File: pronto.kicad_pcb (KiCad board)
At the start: 2 copper layers, 53.3 x 81.3 mm, 400 parts

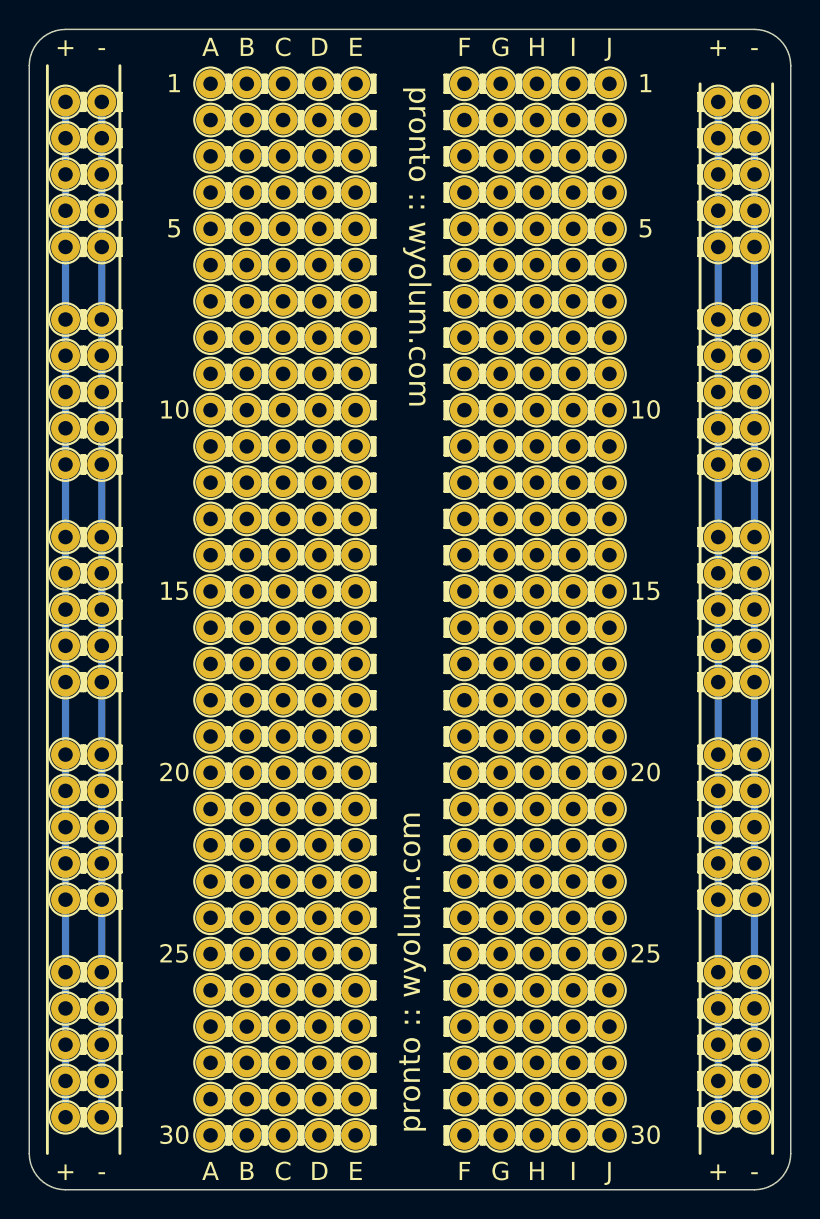
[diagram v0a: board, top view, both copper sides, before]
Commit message: front legend update
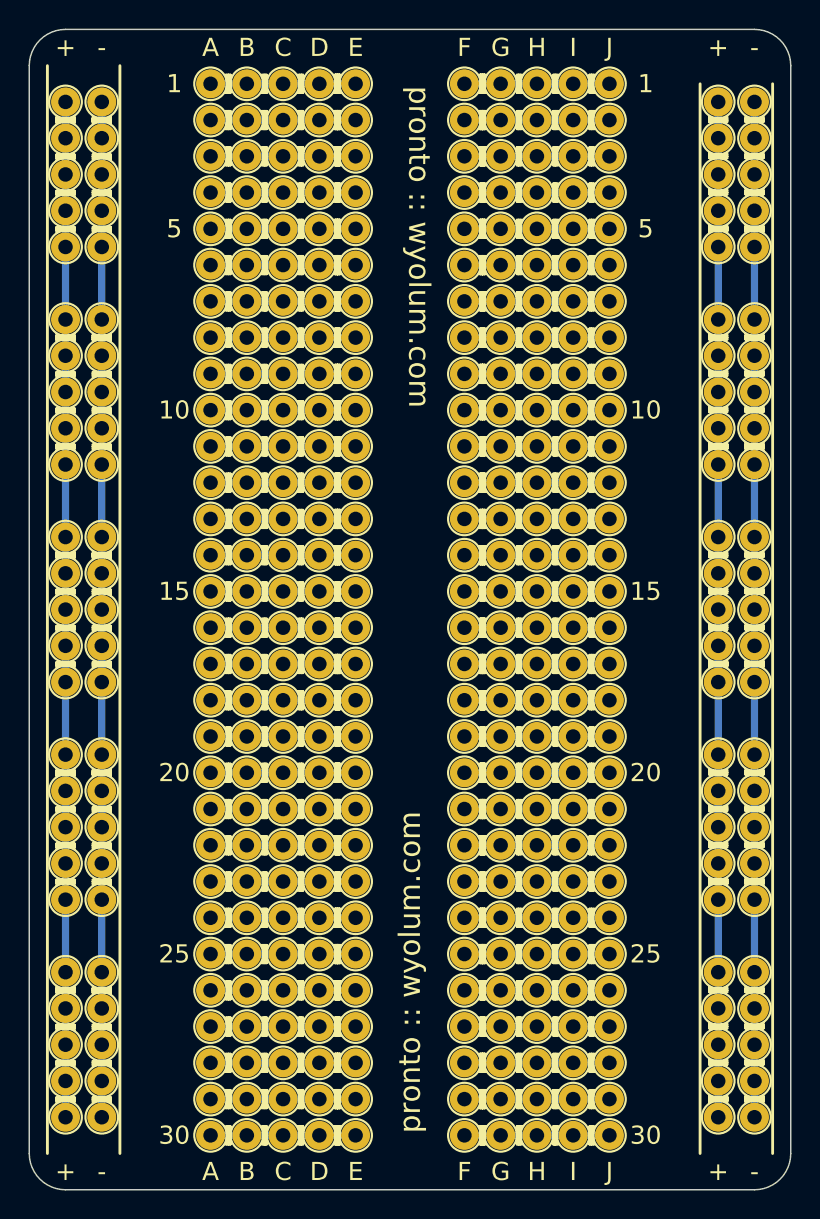
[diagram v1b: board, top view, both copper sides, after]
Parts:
- turned 1pin to 90 degrees (x13)
- turned 1pin to 270 degrees (x2)
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
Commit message: modified layout
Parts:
- added 1pin: VAL**, proto:1pin, F.Cu at (96.5, 116.8)
- added 1pin: VAL**, proto:1pin, F.Cu at (139.7, 71.1)
- added 1pin: VAL**, proto:1pin, F.Cu at (142.2, 55.9)
- added 1pin: VAL**, proto:1pin, F.Cu at (139.7, 55.9)
- added 1pin: VAL**, proto:1pin, F.Cu at (96.5, 101.6)
- added 1pin: VAL**, proto:1pin, F.Cu at (94.0, 101.6)
- added 1pin: VAL**, proto:1pin, F.Cu at (96.5, 86.4)
- added 1pin: VAL**, proto:1pin, F.Cu at (94.0, 86.4)
- added 1pin: VAL**, proto:1pin, F.Cu at (96.5, 71.1)
- added 1pin: VAL**, proto:1pin, F.Cu at (94.0, 71.1)
- added 1pin: VAL**, proto:1pin, F.Cu at (96.5, 55.9)
- added 1pin: VAL**, proto:1pin, F.Cu at (94.0, 116.8)
- added 1pin: VAL**, proto:1pin, F.Cu at (94.0, 55.9)
- added 1pin: VAL**, proto:1pin, F.Cu at (119.4, 116.8)
- added 1pin: VAL**, proto:1pin, F.Cu at (116.8, 116.8)
- added 1pin: VAL**, proto:1pin, F.Cu at (119.4, 101.6)
- added 1pin: VAL**, proto:1pin, F.Cu at (116.8, 101.6)
- added 1pin: VAL**, proto:1pin, F.Cu at (119.4, 86.4)
- added 1pin: VAL**, proto:1pin, F.Cu at (116.8, 86.4)
- added 1pin: VAL**, proto:1pin, F.Cu at (119.4, 71.1)
- added 1pin: VAL**, proto:1pin, F.Cu at (116.8, 71.1)
- added 1pin: VAL**, proto:1pin, F.Cu at (119.4, 55.9)
- added 1pin: VAL**, proto:1pin, F.Cu at (142.2, 116.8)
- added 1pin: VAL**, proto:1pin, F.Cu at (116.8, 55.9)
- added 1pin: VAL**, proto:1pin, F.Cu at (116.8, 73.7)
- added 1pin: VAL**, proto:1pin, F.Cu at (119.4, 73.7)
- added 1pin: VAL**, proto:1pin, F.Cu at (116.8, 66.0)
- added 1pin: VAL**, proto:1pin, F.Cu at (119.4, 66.0)
- added 1pin: VAL**, proto:1pin, F.Cu at (119.4, 68.6)
- added 1pin: VAL**, proto:1pin, F.Cu at (116.8, 68.6)
- added 1pin: VAL**, proto:1pin, F.Cu at (116.8, 58.4)
- added 1pin: VAL**, proto:1pin, F.Cu at (119.4, 58.4)
- added 1pin: VAL**, proto:1pin, F.Cu at (116.8, 61.0)
- added 1pin: VAL**, proto:1pin, F.Cu at (139.7, 116.8)
- added 1pin: VAL**, proto:1pin, F.Cu at (119.4, 61.0)
- added 1pin: VAL**, proto:1pin, F.Cu at (119.4, 63.5)
- added 1pin: VAL**, proto:1pin, F.Cu at (116.8, 63.5)
- added 1pin: VAL**, proto:1pin, F.Cu at (116.8, 43.2)
- added 1pin: VAL**, proto:1pin, F.Cu at (119.4, 43.2)
- added 1pin: VAL**, proto:1pin, F.Cu at (116.8, 48.3)
- added 1pin: VAL**, proto:1pin, F.Cu at (119.4, 48.3)
- added 1pin: VAL**, proto:1pin, F.Cu at (119.4, 45.7)
- added 1pin: VAL**, proto:1pin, F.Cu at (116.8, 45.7)
- added 1pin: VAL**, proto:1pin, F.Cu at (116.8, 50.8)
- added 1pin: VAL**, proto:1pin, F.Cu at (142.2, 101.6)
- added 1pin: VAL**, proto:1pin, F.Cu at (119.4, 50.8)
- added 1pin: VAL**, proto:1pin, F.Cu at (119.4, 53.3)
- added 1pin: VAL**, proto:1pin, F.Cu at (116.8, 53.3)
- added 1pin: VAL**, proto:1pin, F.Cu at (116.8, 94.0)
- added 1pin: VAL**, proto:1pin, F.Cu at (119.4, 94.0)
- added 1pin: VAL**, proto:1pin, F.Cu at (119.4, 91.4)
- added 1pin: VAL**, proto:1pin, F.Cu at (116.8, 91.4)
- added 1pin: VAL**, proto:1pin, F.Cu at (119.4, 88.9)
- added 1pin: VAL**, proto:1pin, F.Cu at (116.8, 88.9)
- added 1pin: VAL**, proto:1pin, F.Cu at (116.8, 78.7)
- added 1pin: VAL**, proto:1pin, F.Cu at (139.7, 101.6)
- added 1pin: VAL**, proto:1pin, F.Cu at (119.4, 78.7)
- added 1pin: VAL**, proto:1pin, F.Cu at (119.4, 76.2)
- added 1pin: VAL**, proto:1pin, F.Cu at (116.8, 76.2)
- added 1pin: VAL**, proto:1pin, F.Cu at (116.8, 81.3)
- added 1pin: VAL**, proto:1pin, F.Cu at (119.4, 81.3)
- added 1pin: VAL**, proto:1pin, F.Cu at (119.4, 83.8)
- added 1pin: VAL**, proto:1pin, F.Cu at (116.8, 83.8)
- added 1pin: VAL**, proto:1pin, F.Cu at (116.8, 104.1)
- added 1pin: VAL**, proto:1pin, F.Cu at (119.4, 104.1)
- added 1pin: VAL**, proto:1pin, F.Cu at (116.8, 96.5)
- added 1pin: VAL**, proto:1pin, F.Cu at (142.2, 86.4)
- added 1pin: VAL**, proto:1pin, F.Cu at (119.4, 96.5)
- added 1pin: VAL**, proto:1pin, F.Cu at (119.4, 99.1)
- added 1pin: VAL**, proto:1pin, F.Cu at (116.8, 99.1)
- added 1pin: VAL**, proto:1pin, F.Cu at (116.8, 109.2)
- added 1pin: VAL**, proto:1pin, F.Cu at (119.4, 109.2)
- added 1pin: VAL**, proto:1pin, F.Cu at (119.4, 106.7)
- added 1pin: VAL**, proto:1pin, F.Cu at (116.8, 106.7)
- added 1pin: VAL**, proto:1pin, F.Cu at (116.8, 111.8)
- added 1pin: VAL**, proto:1pin, F.Cu at (119.4, 111.8)
- added 1pin: VAL**, proto:1pin, F.Cu at (119.4, 114.3)
- added 1pin: VAL**, proto:1pin, F.Cu at (139.7, 86.4)
- added 1pin: VAL**, proto:1pin, F.Cu at (116.8, 114.3)
- added 1pin: VAL**, proto:1pin, F.Cu at (142.2, 71.1)
- moved 1pin 1.27 mm to (96.5, 96.5)
- moved 1pin 1.27 mm to (94.0, 96.5)
- moved 1pin 1.27 mm to (94.0, 83.8)
- moved 1pin 1.27 mm to (96.5, 83.8)
- moved 1pin 1.27 mm to (96.5, 78.7)
- moved 1pin 1.27 mm to (94.0, 78.7)
- moved 1pin 1.27 mm to (96.5, 73.7), turned to 180 degrees
- moved 1pin 1.27 mm to (94.0, 73.7), turned to 180 degrees
- moved 1pin 1.27 mm to (142.2, 73.7)
- moved 1pin 1.27 mm to (139.7, 73.7)
- moved 1pin 1.27 mm to (142.2, 78.7)
- moved 1pin 1.27 mm to (139.7, 78.7)
- moved 1pin 1.27 mm to (139.7, 83.8), turned to 0 degrees
- moved 1pin 1.27 mm to (142.2, 83.8), turned to 0 degrees
- moved 1pin 1.27 mm to (142.2, 96.5)
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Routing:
- net (no net): track 904.2 -> 1056.6 mm
